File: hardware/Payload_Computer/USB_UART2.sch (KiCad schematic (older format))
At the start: 11 parts

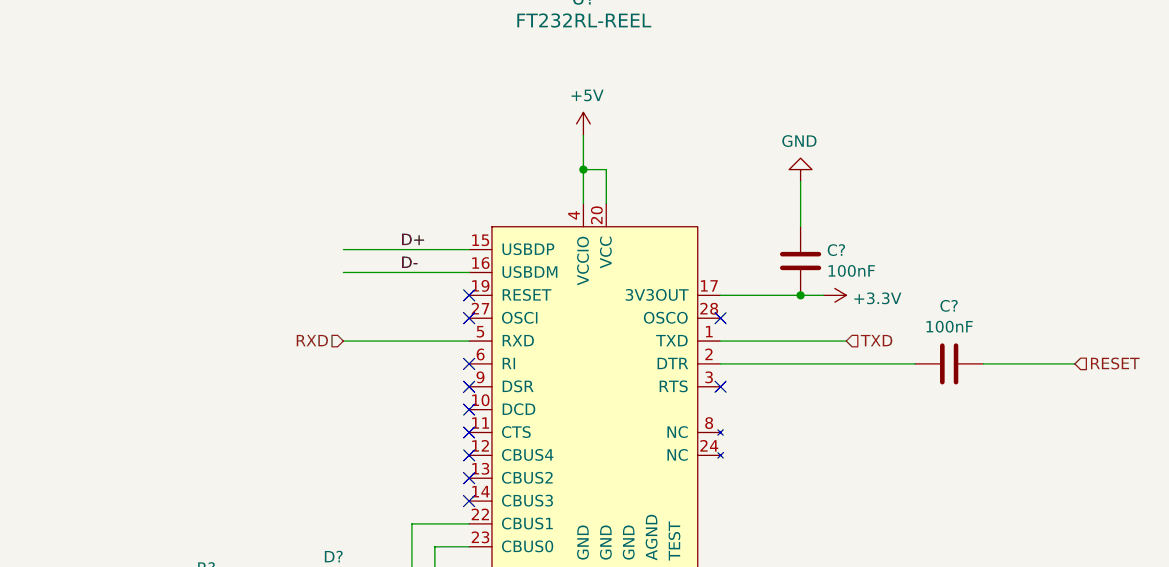
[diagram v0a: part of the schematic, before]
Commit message: Added reset circuits
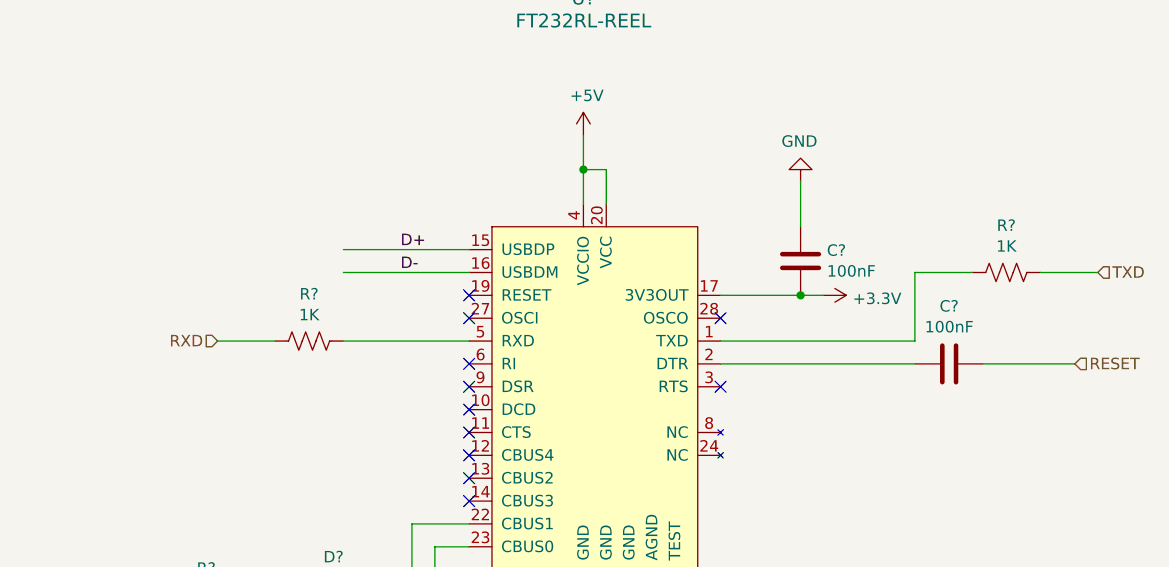
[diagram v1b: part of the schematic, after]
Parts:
- added R? (x2): 1K, symbol Device:R_US
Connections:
- wire segments 46 -> 50
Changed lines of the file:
@@
 $Descr A4 11693 8268
 encoding utf-8
-Sheet 7 7
+Sheet 7 9
 Title ""
 Date ""
@@
 Text Label 7150 3050 0    50   ~ 0
 D-
-Text HLabel 6900 3350 0    50   Input ~ 0
+Text HLabel 6350 3350 0    50   Input ~ 0
 RXD
-Text HLabel 9100 3350 2    50   Input ~ 0
+Text HLabel 10200 3050 2    50   Input ~ 0
 TXD
-Wire Wire Line
-	8550 3350 9100 3350
 Wire Wire Line
 	7450 3350 6900 3350
@@
 NoConn ~ 7450 3950
 NoConn ~ 7450 4050
+$Comp
+L Device:R_US R?
+U 1 1 5F8E6C6D
+P 6750 3350
+F 0 "R?" V 6545 3350 50  0000 C CNN
+F 1 "1K" V 6636 3350 50  0000 C CNN
+F 2 "" V 6790 3340 50  0001 C CNN
+F 3 "~" H 6750 3350 50  0001 C CNN
+	1    6750 3350
+	0    1    1    0
+$EndComp
+Wire Wire Line
+	6600 3350 6350 3350
+Wire Wire Line
+	9400 3350 9400 3050
+Wire Wire Line
+	9400 3050 9650 3050
+Wire Wire Line
+	8550 3350 9400 3350
+$Comp
+L Device:R_US R?
+U 1 1 5F8E8DCF
+P 9800 3050
+F 0 "R?" V 9595 3050 50  0000 C CNN
+F 1 "1K" V 9686 3050 50  0000 C CNN
+F 2 "" V 9840 3040 50  0001 C CNN
+F 3 "~" H 9800 3050 50  0001 C CNN
+	1    9800 3050
+	0    1    1    0
+$EndComp
+Wire Wire Line
+	9950 3050 10200 3050
 $EndSCHEMATC

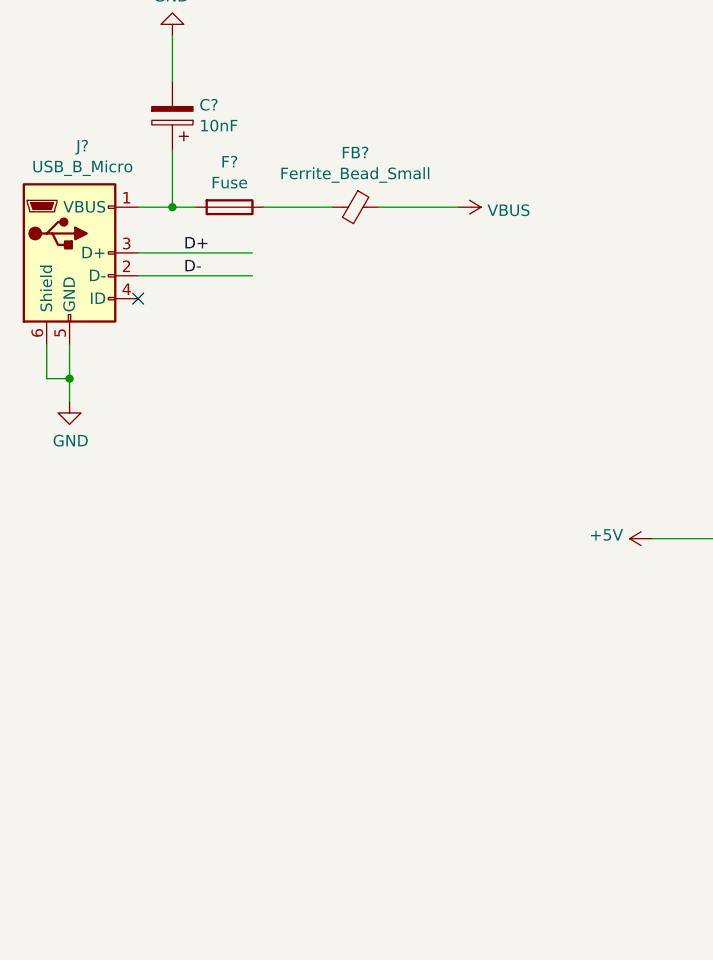
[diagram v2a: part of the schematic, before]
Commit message: Finished ICSP. Added a few leds and filtering caps
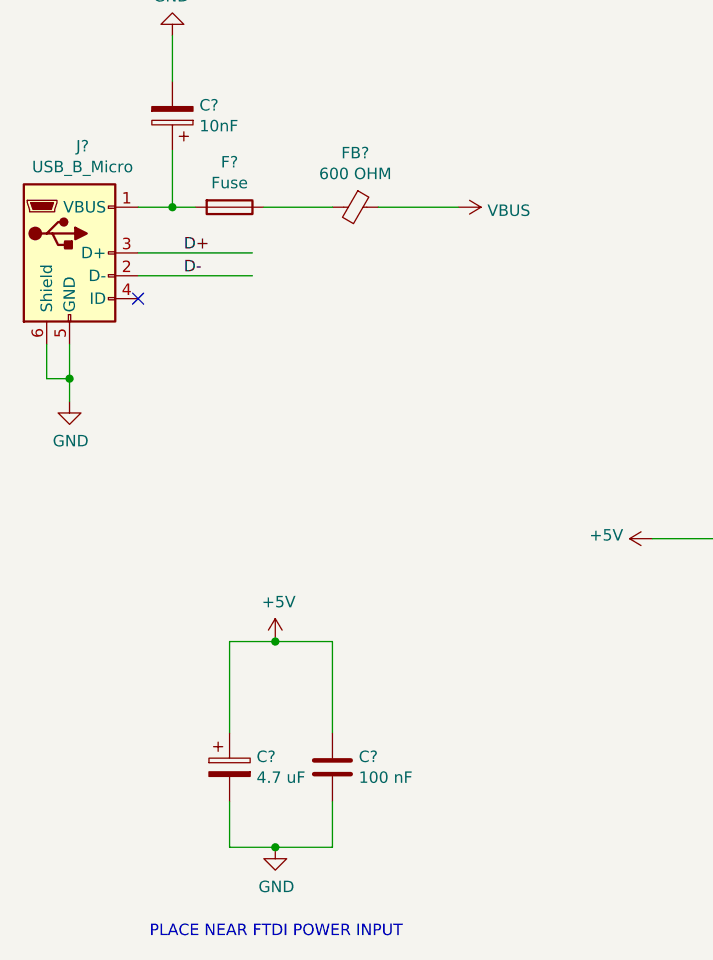
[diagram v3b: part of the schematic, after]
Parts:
- added C?: 100 nF, symbol Device:C
- added C?: 4.7 uF, symbol Device:CP
- FB?: value Ferrite_Bead_Small -> 600 OHM
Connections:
- wire segments 50 -> 58
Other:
- note added: "PLACE NEAR FTDI POWER INPUT\n"
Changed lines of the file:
@@
 $Descr A4 11693 8268
 encoding utf-8
-Sheet 7 11
+Sheet 7 13
 Title ""
 Date ""
@@
 	3600 3300 3700 3300
 $Comp
-L power:GND #PWR?
+L power:GND #PWR0117
 U 1 1 5F874593
 P 3600 2550
-F 0 "#PWR?" H 3600 2300 50  0001 C CNN
+F 0 "#PWR0117" H 3600 2300 50  0001 C CNN
 F 1 "GND" H 3605 2377 50  0000 C CNN
 F 2 "" H 3600 2550 50  0001 C CNN
@@
 P 4400 3300
 F 0 "FB?" V 4163 3300 50  0000 C CNN
-F 1 "Ferrite_Bead_Small" V 4254 3300 50  0000 C CNN
+F 1 "600 OHM" V 4254 3300 50  0000 C CNN
 F 2 "" V 4330 3300 50  0001 C CNN
 F 3 "~" H 4400 3300 50  0001 C CNN
@@
 	4000 3300 4300 3300
 $Comp
-L power:VBUS #PWR?
+L power:VBUS #PWR0118
 U 1 1 5F8745A1
 P 4850 3300
-F 0 "#PWR?" H 4850 3150 50  0001 C CNN
+F 0 "#PWR0118" H 4850 3150 50  0001 C CNN
 F 1 "VBUS" V 4865 3428 50  0000 L CNN
 F 2 "" H 4850 3300 50  0001 C CNN
@@
 	4500 3300 4850 3300
 $Comp
-L power:GND #PWR?
+L power:GND #PWR0119
 U 1 1 5F8745A8
 P 3150 4150
-F 0 "#PWR?" H 3150 3900 50  0001 C CNN
+F 0 "#PWR0119" H 3150 3900 50  0001 C CNN
 F 1 "GND" H 3155 3977 50  0000 C CNN
 F 2 "" H 3150 4150 50  0001 C CNN
@@
 NoConn ~ 3450 3700
 $Comp
-L power:+5V #PWR?
+L power:+5V #PWR0120
 U 1 1 5F8745B8
 P 7950 2450
-F 0 "#PWR?" H 7950 2300 50  0001 C CNN
+F 0 "#PWR0120" H 7950 2300 50  0001 C CNN
 F 1 "+5V" H 7965 2623 50  0000 C CNN
 F 2 "" H 7950 2450 50  0001 C CNN
@@
 	7950 2600 7950 2450
 $Comp
-L power:GND #PWR?
+L power:GND #PWR0121
 U 1 1 5F8745C3
 P 7950 4750
-F 0 "#PWR?" H 7950 4500 50  0001 C CNN
+F 0 "#PWR0121" H 7950 4500 50  0001 C CNN
 F 1 "GND" H 7955 4577 50  0000 C CNN
 F 2 "" H 7950 4750 50  0001 C CNN
@@
 	8550 3150 8900 3150
 $Comp
-L power:+3.3V #PWR?
+L power:+3.3V #PWR0122
 U 1 1 5F8745F7
 P 9000 3150
-F 0 "#PWR?" H 9000 3000 50  0001 C CNN
+F 0 "#PWR0122" H 9000 3000 50  0001 C CNN
 F 1 "+3.3V" V 9015 3278 50  0000 L CNN
 F 2 "" H 9000 3150 50  0001 C CNN
@@
 Connection ~ 8900 3150
 $Comp
-L power:GND #PWR?
+L power:GND #PWR0123
 U 1 1 5F8745FF
 P 8900 2650
-F 0 "#PWR?" H 8900 2400 50  0001 C CNN
+F 0 "#PWR0123" H 8900 2400 50  0001 C CNN
 F 1 "GND" H 8905 2477 50  0000 C CNN
 F 2 "" H 8900 2650 50  0001 C CNN
@@
 	6700 4950 6450 4950
 $Comp
-L power:+5V #PWR?
+L power:+5V #PWR0124
 U 1 1 5F874626
 P 5700 4750
-F 0 "#PWR?" H 5700 4600 50  0001 C CNN
+F 0 "#PWR0124" H 5700 4600 50  0001 C CNN
 F 1 "+5V" V 5715 4878 50  0000 L CNN
 F 2 "" H 5700 4750 50  0001 C CNN
@@
 Wire Wire Line
 	9950 3050 10200 3050
+$Comp
+L Device:C C?
+U 1 1 5F98A895
+P 4300 5750
+F 0 "C?" H 4415 5796 50  0000 L CNN
+F 1 "100 nF" H 4415 5705 50  0000 L CNN
+F 2 "" H 4338 5600 50  0001 C CNN
+F 3 "~" H 4300 5750 50  0001 C CNN
+	1    4300 5750
+	1    0    0    -1
+$EndComp
+$Comp
+L Device:CP C?
+U 1 1 5F98AD93
+P 3850 5750
+F 0 "C?" H 3968 5796 50  0000 L CNN
+F 1 "4.7 uF" H 3968 5705 50  0000 L CNN
+F 2 "" H 3888 5600 50  0001 C CNN
+F 3 "~" H 3850 5750 50  0001 C CNN
+	1    3850 5750
+	1    0    0    -1
+$EndComp
+$Comp
+L power:+5V #PWR?
+U 1 1 5F98B9B9
+P 4050 5200
+F 0 "#PWR?" H 4050 5050 50  0001 C CNN
+F 1 "+5V" H 4065 5373 50  0000 C CNN
+F 2 "" H 4050 5200 50  0001 C CNN
+F 3 "" H 4050 5200 50  0001 C CNN
+	1    4050 5200
+	1    0    0    -1
+$EndComp
+Wire Wire Line
+	3850 5600 3850 5200
+Wire Wire Line
+	3850 5200 4050 5200
+Wire Wire Line
+	4300 5600 4300 5200
+Wire Wire Line
+	4300 5200 4050 5200
+Connection ~ 4050 5200
+$Comp
+L power:GND #PWR?
+U 1 1 5F98E99D
+P 4050 6100
+F 0 "#PWR?" H 4050 5850 50  0001 C CNN
+F 1 "GND" H 4055 5927 50  0000 C CNN
+F 2 "" H 4050 6100 50  0001 C CNN
+F 3 "" H 4050 6100 50  0001 C CNN
+	1    4050 6100
+	1    0    0    -1
+$EndComp
+Wire Wire Line
+	3850 5900 3850 6100
+Wire Wire Line
+	3850 6100 4050 6100
+Wire Wire Line
+	4300 5900 4300 6100
+Wire Wire Line
+	4300 6100 4050 6100
+Connection ~ 4050 6100
+Text Notes 3500 6500 0    50   ~ 0
+PLACE NEAR FTDI POWER INPUT\n
 $EndSCHEMATC
